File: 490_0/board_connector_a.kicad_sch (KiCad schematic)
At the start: 20 parts, among them J16 DF40HC(3.0)-100DS-0.4V(58), J17 DF40HC(3.0)-100DS-0.4V(58), J21 TS-102-G-A, Q6 BSS84, SW2 TL1105LF160Q, SW3 TL1105LF160Q, SW4 TL1105LF160Q, SW5 TL1105LF160Q, SW6 TL1105LF160Q, SW7 TL1105LF160Q

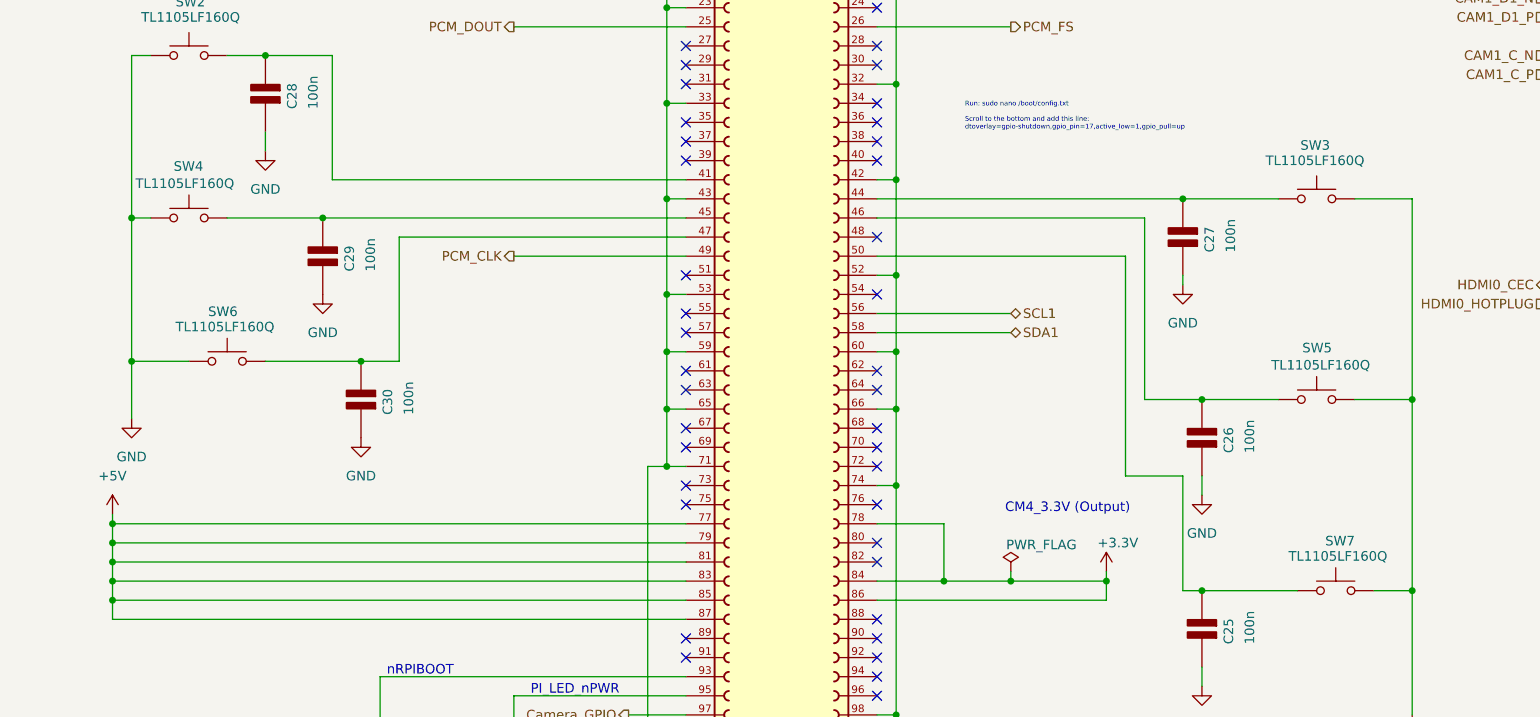
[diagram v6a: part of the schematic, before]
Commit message: Changed pin assignment for the buttons on PCB1 in the schematic
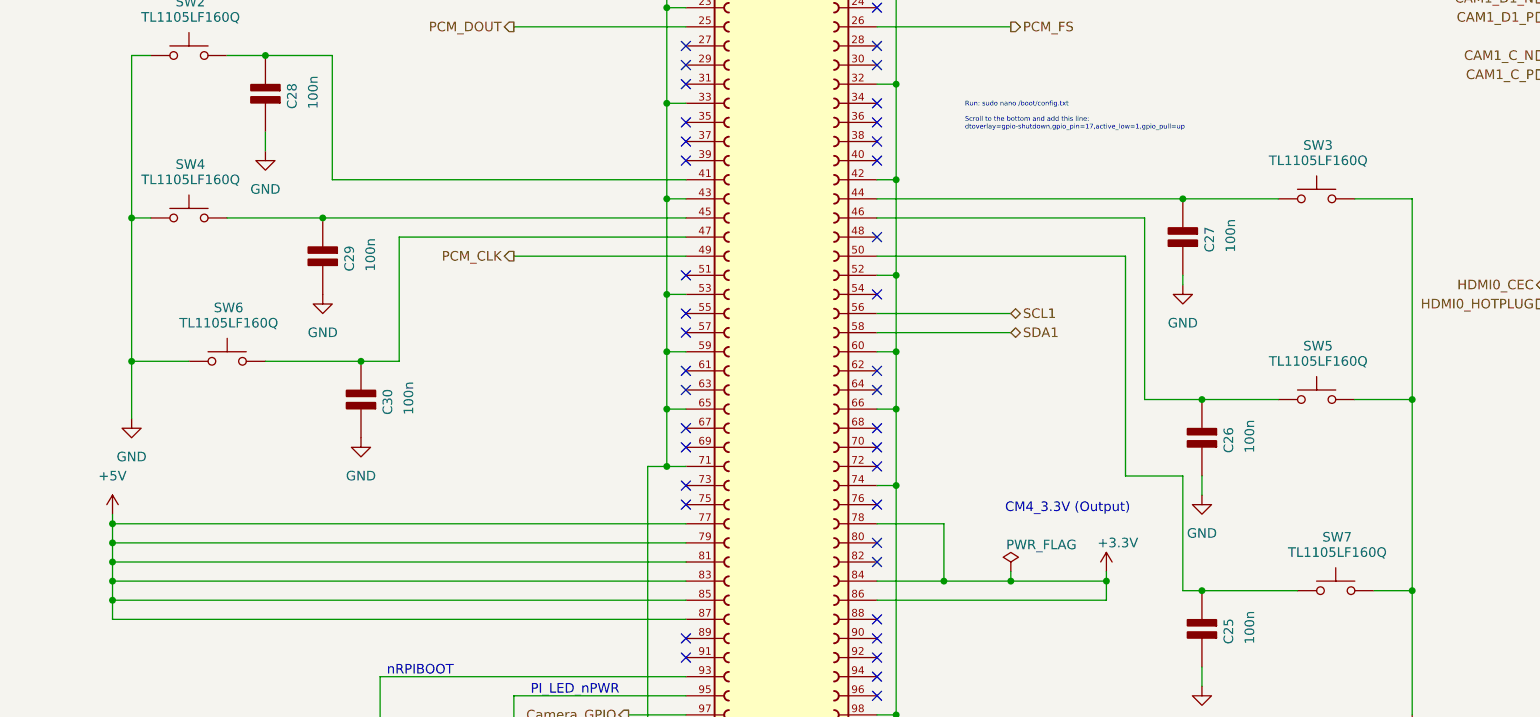
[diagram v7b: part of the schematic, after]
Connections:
- net GND: now also SW2.3, SW3.2, SW4.3, SW5.2, SW6.3, SW7.2; no longer SW2.1, SW3.1, SW4.1, SW5.1, SW6.1, SW7.1
- net at C27.2 (-), J16.44: now also SW3.3; no longer SW3.2
- net at C26.2 (-), J16.46: now also SW5.3; no longer SW5.2
- net at C25.2 (-), J16.50: now also SW7.3; no longer SW7.2
